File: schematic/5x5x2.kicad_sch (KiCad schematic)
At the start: 164 parts, among them J1 SW Debug, J2 USB_C_Receptacle_USB2.0, SW1 SW, SW11 SW, SW12 SW, SW13 SW, SW14 SW, SW15 SW, SW21 SW, SW22 SW, SW23 SW, SW24 SW, SW25 SW, SW31 SW, SW32 SW, SW33 SW, SW34 SW, SW35 SW, SW41 SW, SW42 SW, SW43 SW, SW44 SW, SW45 SW, SW51 SW, SW52 SW, SW53 SW, SW54 SW, SW55 SW, SW6 ALPS_EC11, U1 SRV0504, U2 STM32F103C8, U3 LD1117S33CTR, Y1 16M

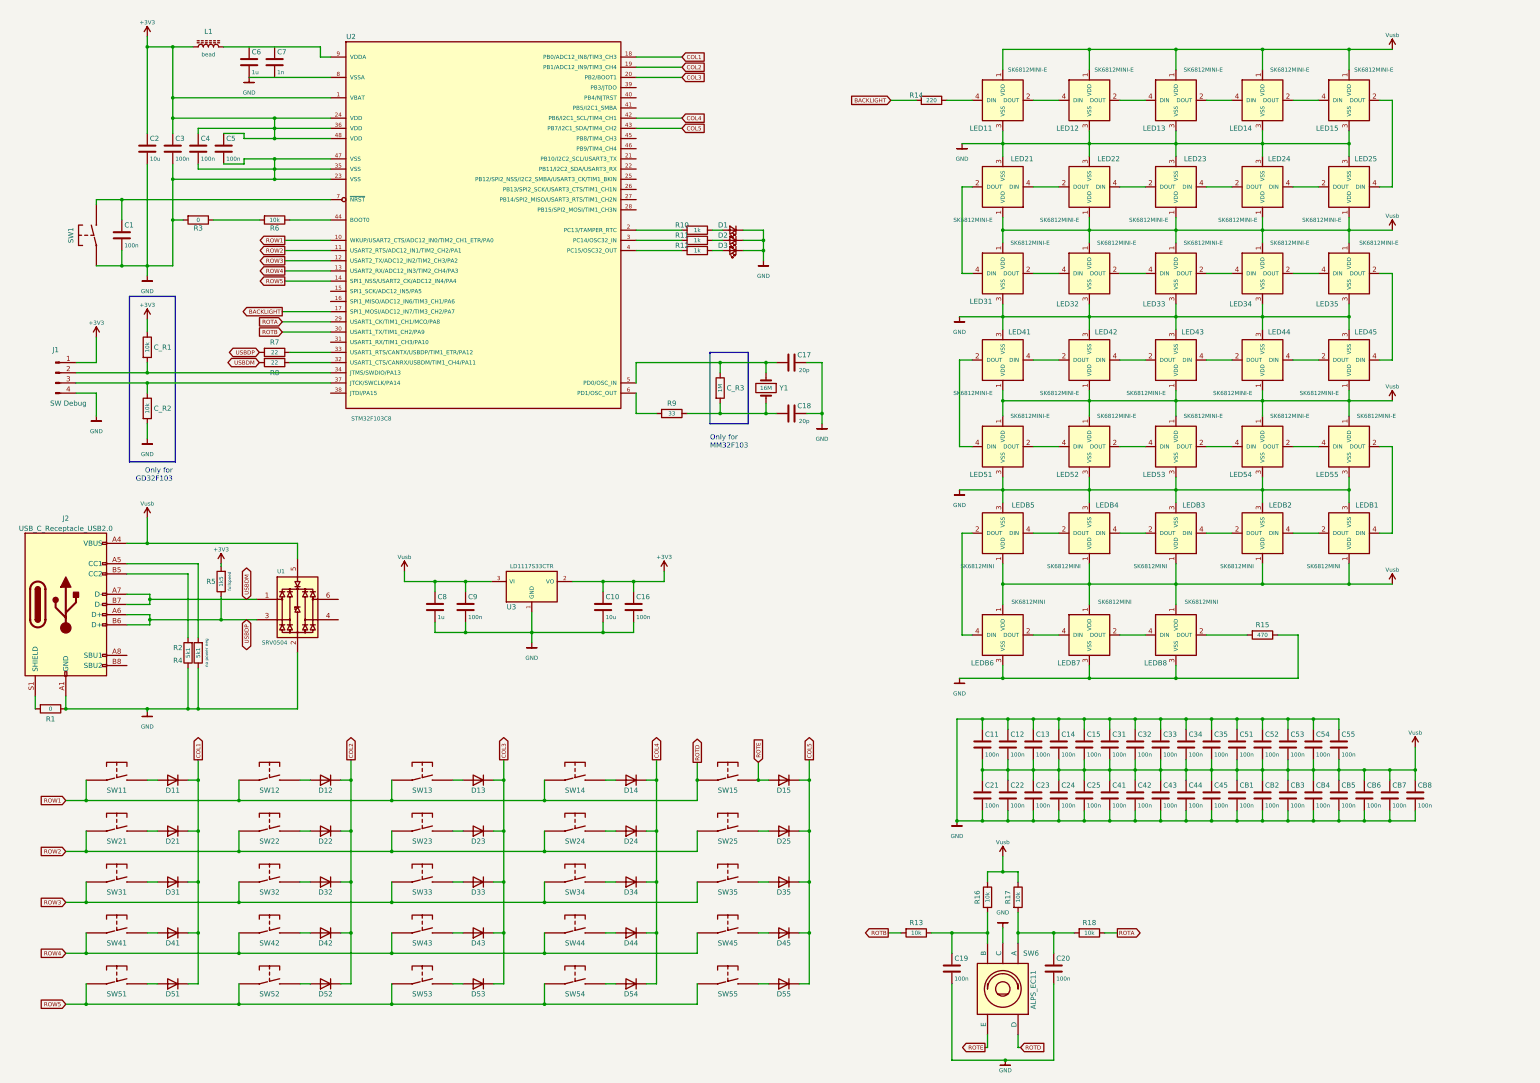
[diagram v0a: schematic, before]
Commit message: Added board interconnectors
And started redoing the board interconnects -- the previous solution
lacked symmetry and elegance (= looked like a dog's breakfast).
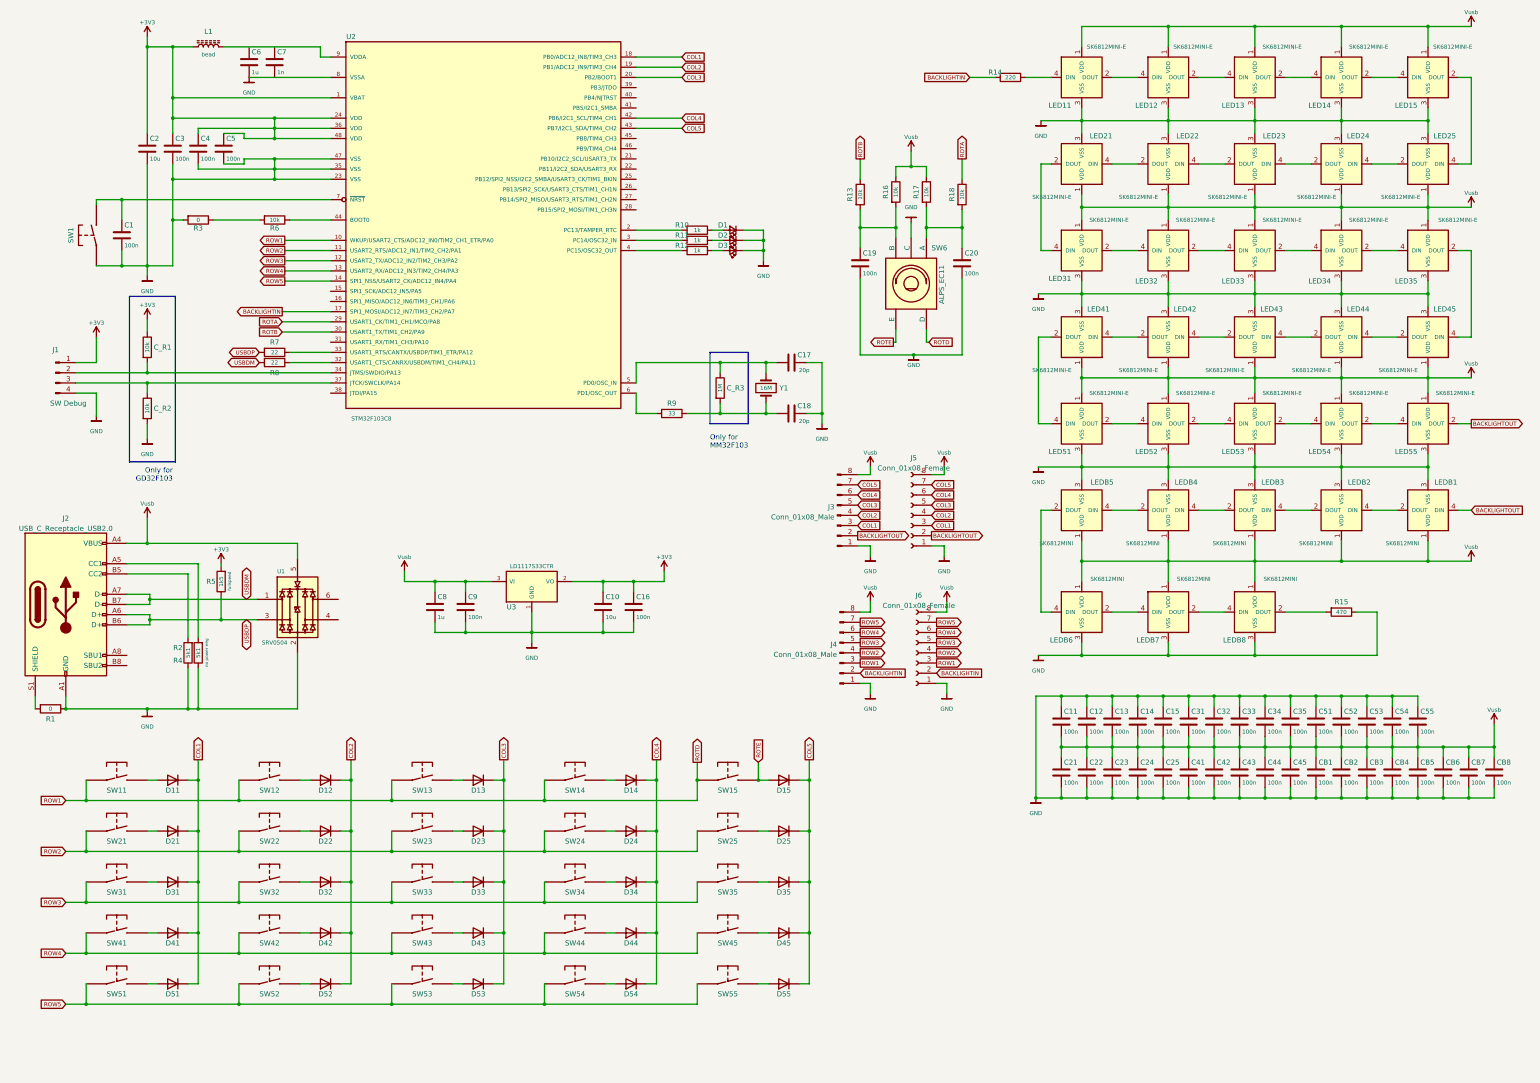
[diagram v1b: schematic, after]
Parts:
- added J3, J4: Conn_01x08_Male, Connector_PinSocket_2.54mm:PinSocket_1x08_P2.54mm_Vertical, symbol Connector:Conn_01x08_Male
- added J5, J6: Conn_01x08_Female, Connector_PinSocket_2.54mm:PinSocket_1x08_P2.54mm_Vertical, symbol Connector:Conn_01x08_Female
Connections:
- net COL1: now also J3.3 (Pin_3), J5.3 (Pin_3)
- net COL2: now also J3.4 (Pin_4), J5.4 (Pin_4)
- net COL3: now also J3.5 (Pin_5), J5.5 (Pin_5)
- net COL4: now also J3.6 (Pin_6), J5.6 (Pin_6)
- net COL5: now also J3.7 (Pin_7), J5.7 (Pin_7)
- net GND: now also J3.1 (Pin_1), J4.1 (Pin_1), J5.1 (Pin_1), J6.1 (Pin_1)
- net ROTB: now also R13.1; no longer R13.2
- net ROTD: now also J4.3 (Pin_3), J6.3 (Pin_3)
- net ROW2: now also J4.4 (Pin_4), J6.4 (Pin_4)
- net ROW3: now also J4.5 (Pin_5), J6.5 (Pin_5)
- net ROW4: now also J4.6 (Pin_6), J6.6 (Pin_6)
- net ROW5: now also J4.7 (Pin_7), J6.7 (Pin_7)
- net Vusb: now also J3.8 (Pin_8), J4.8 (Pin_8), J5.8 (Pin_8), J6.8 (Pin_8)
- net BACKLIGHTOUT: now reaches LED55.2 (DOUT), LEDB1.4 (DIN)
- net BACKLIGHTOUT: now also J3.2 (Pin_2), J5.2 (Pin_2)
- net at C19.1, R16.2, SW6.B: now also R13.2; no longer R13.1
- net BACKLIGHT renamed BACKLIGHTIN
- net BACKLIGHTIN: now also J4.2 (Pin_2), J6.2 (Pin_2)
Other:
- moved on the sheet: C11, C12, C13, C14, C15, C19, C20, C21, C22, C23, C24, C25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

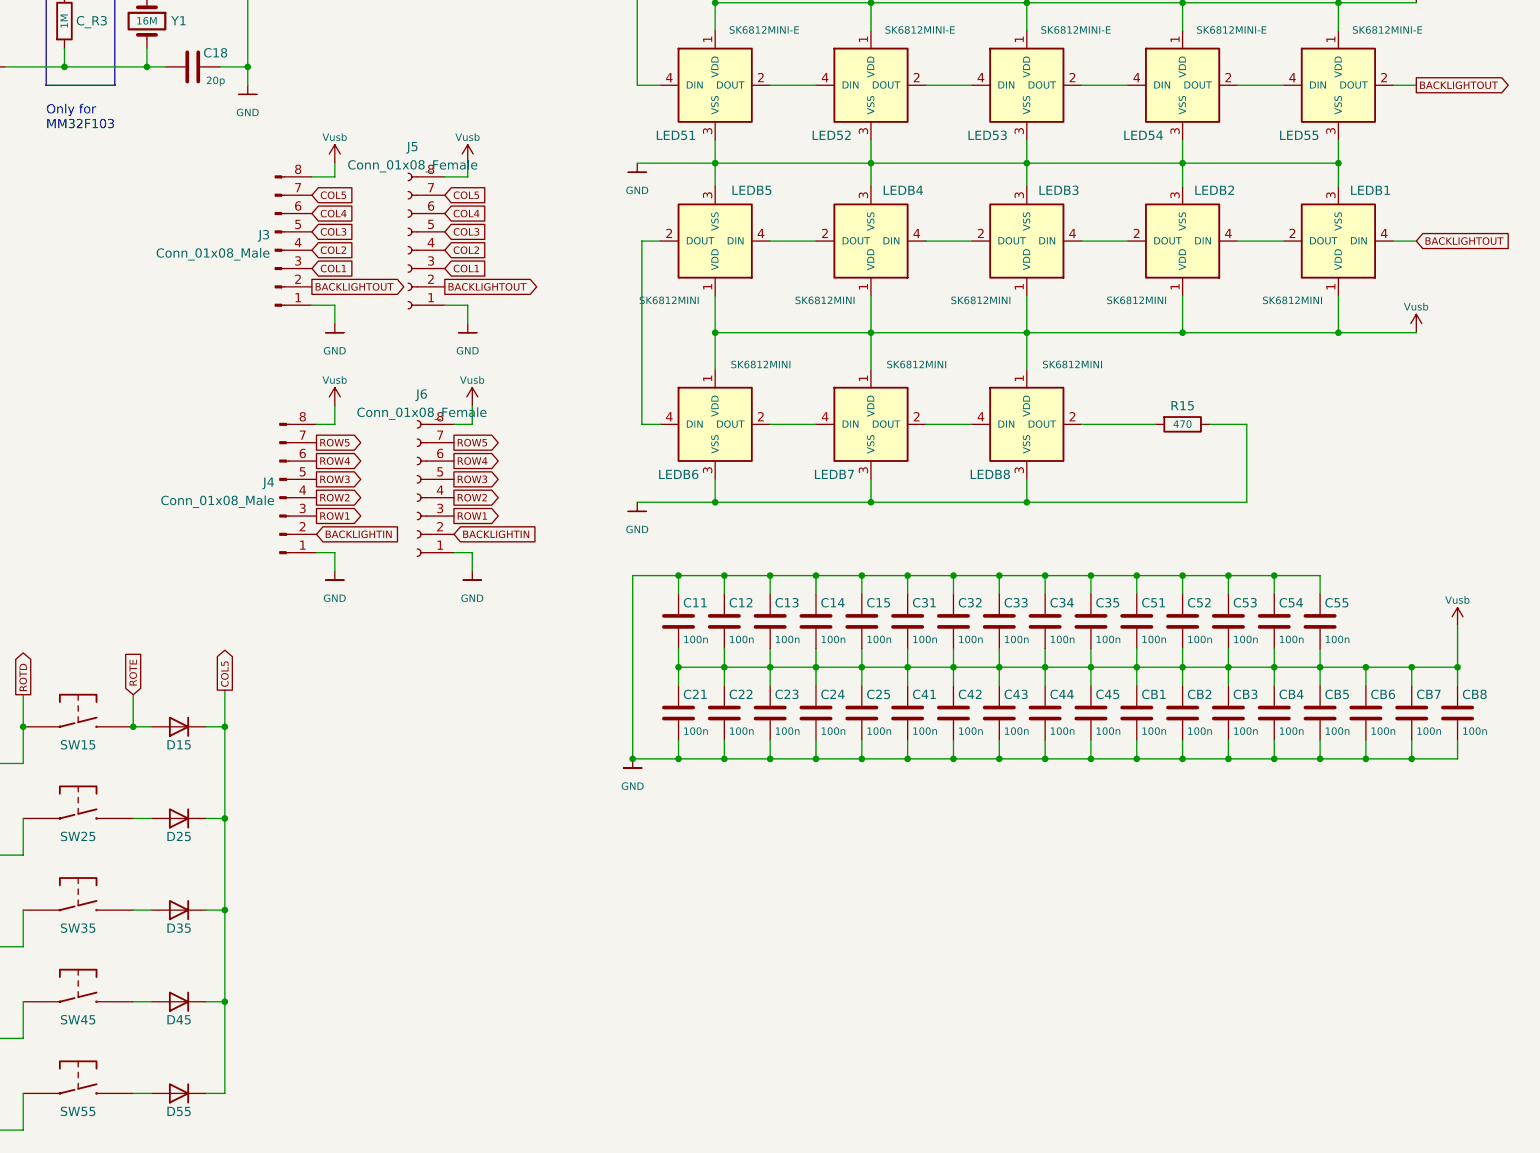
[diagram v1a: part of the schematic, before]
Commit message: Redid board connectors, started 2nd board
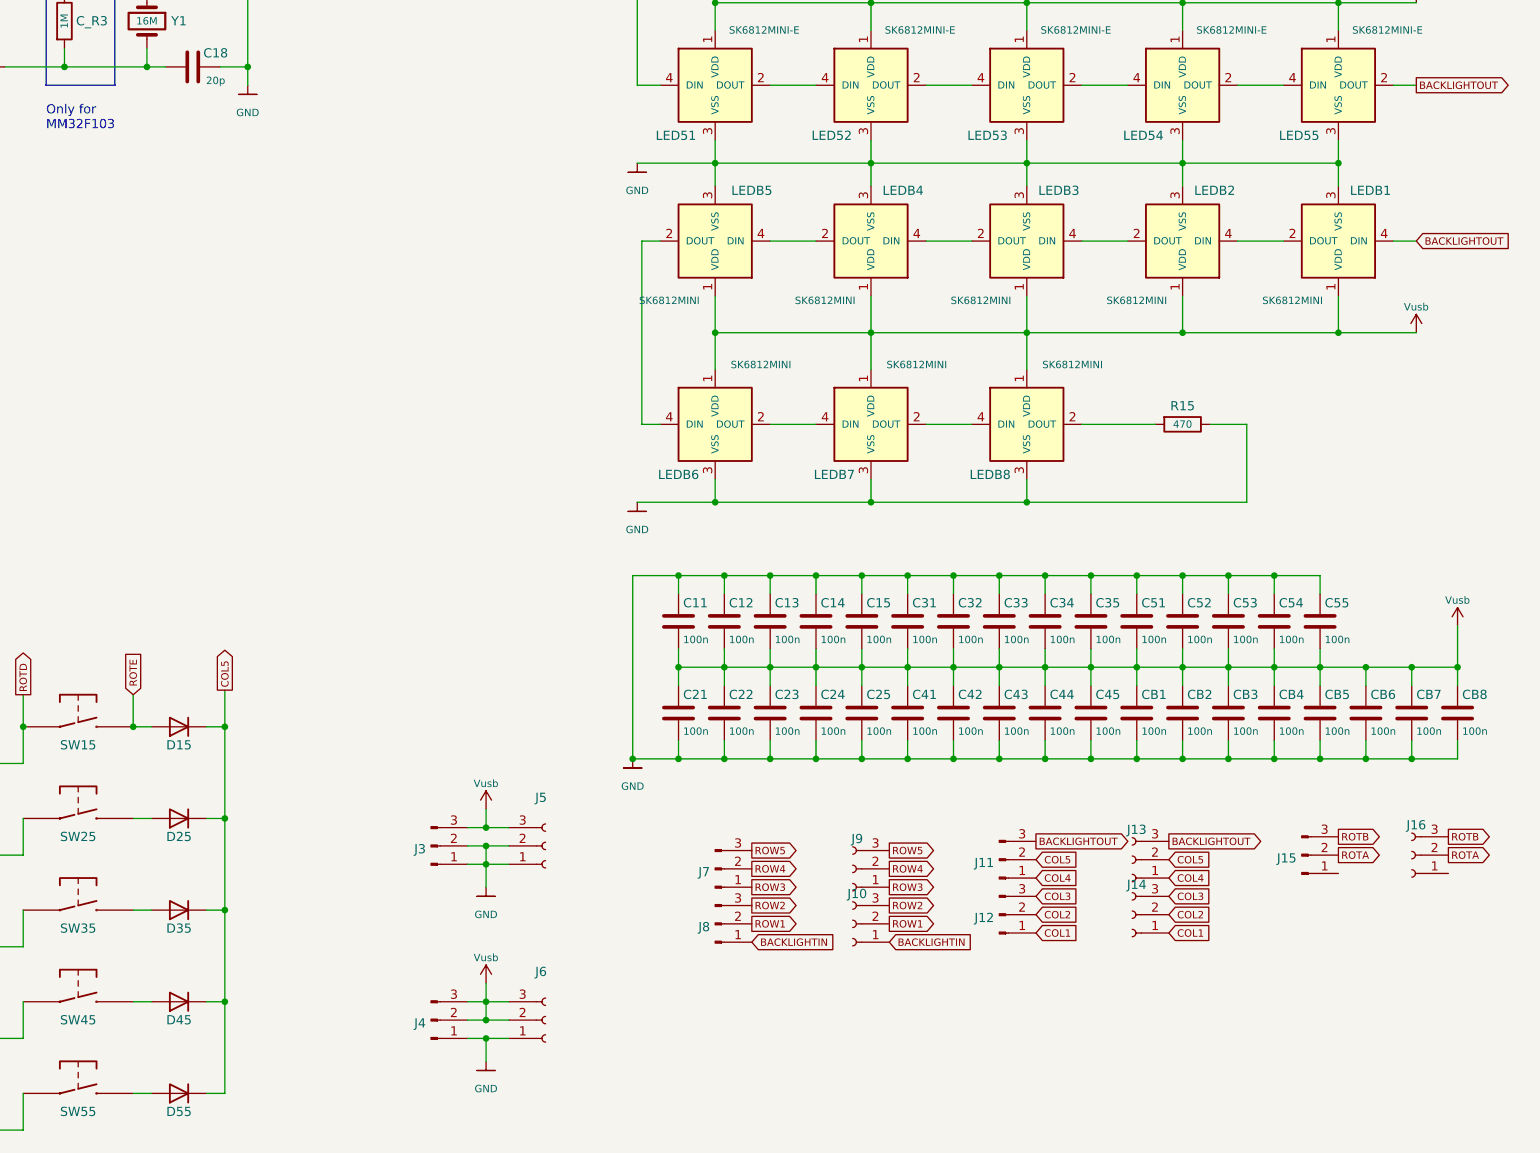
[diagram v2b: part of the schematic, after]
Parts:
- removed J3, J4: Conn_01x08_Male, Connector_PinSocket_2.54mm:PinSocket_1x08_P2.54mm_Vertical, symbol Connector:Conn_01x08_Male
- removed J5, J6: Conn_01x08_Female, Connector_PinSocket_2.54mm:PinSocket_1x08_P2.54mm_Vertical, symbol Connector:Conn_01x08_Female
- added J10, J13, J14, J16, J5, J6, J9: Conn_01x03_Female, Connector_PinSocket_2.54mm:PinSocket_1x03_P2.54mm_Vertical, symbol Connector:Conn_01x03_Female
- added J11, J12, J15, J3, J4, J7, J8: Conn_01x03_Male, Connector_PinSocket_2.54mm:PinSocket_1x03_P2.54mm_Vertical, symbol Connector:Conn_01x03_Male
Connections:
- net BACKLIGHTIN: now also J10.1 (Pin_1), J8.1 (Pin_1)
- net BACKLIGHTOUT: now also J11.3 (Pin_3), J13.3 (Pin_3)
- net COL1: now also J12.1 (Pin_1), J14.1 (Pin_1)
- net COL2: now also J12.2 (Pin_2), J14.2 (Pin_2)
- net COL3: now also J12.3 (Pin_3), J14.3 (Pin_3)
- net COL4: now also J11.1 (Pin_1), J13.1 (Pin_1)
- net COL5: now also J11.2 (Pin_2), J13.2 (Pin_2)
- net GND: now also J3.1 (Pin_1), J3.2 (Pin_2), J4.1 (Pin_1), J5.1 (Pin_1), J5.2 (Pin_2), J6.1 (Pin_1)
- net ROTA: now also J15.2 (Pin_2), J16.2 (Pin_2)
- net ROTB: now also J15.3 (Pin_3), J16.3 (Pin_3)
- net ROTD: now also J10.2 (Pin_2), J8.2 (Pin_2)
- net ROW2: now also J10.3 (Pin_3), J8.3 (Pin_3)
- net ROW3: now also J7.1 (Pin_1), J9.1 (Pin_1)
- net ROW4: now also J7.2 (Pin_2), J9.2 (Pin_2)
- net ROW5: now also J7.3 (Pin_3), J9.3 (Pin_3)
- net Vusb: now also J3.3 (Pin_3), J4.2 (Pin_2), J4.3 (Pin_3), J5.3 (Pin_3), J6.2 (Pin_2), J6.3 (Pin_3)
